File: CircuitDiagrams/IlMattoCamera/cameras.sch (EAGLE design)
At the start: 19 parts, among them Q1 12MHz, U1 ATMEGA644-20PU, X1 SDBMF

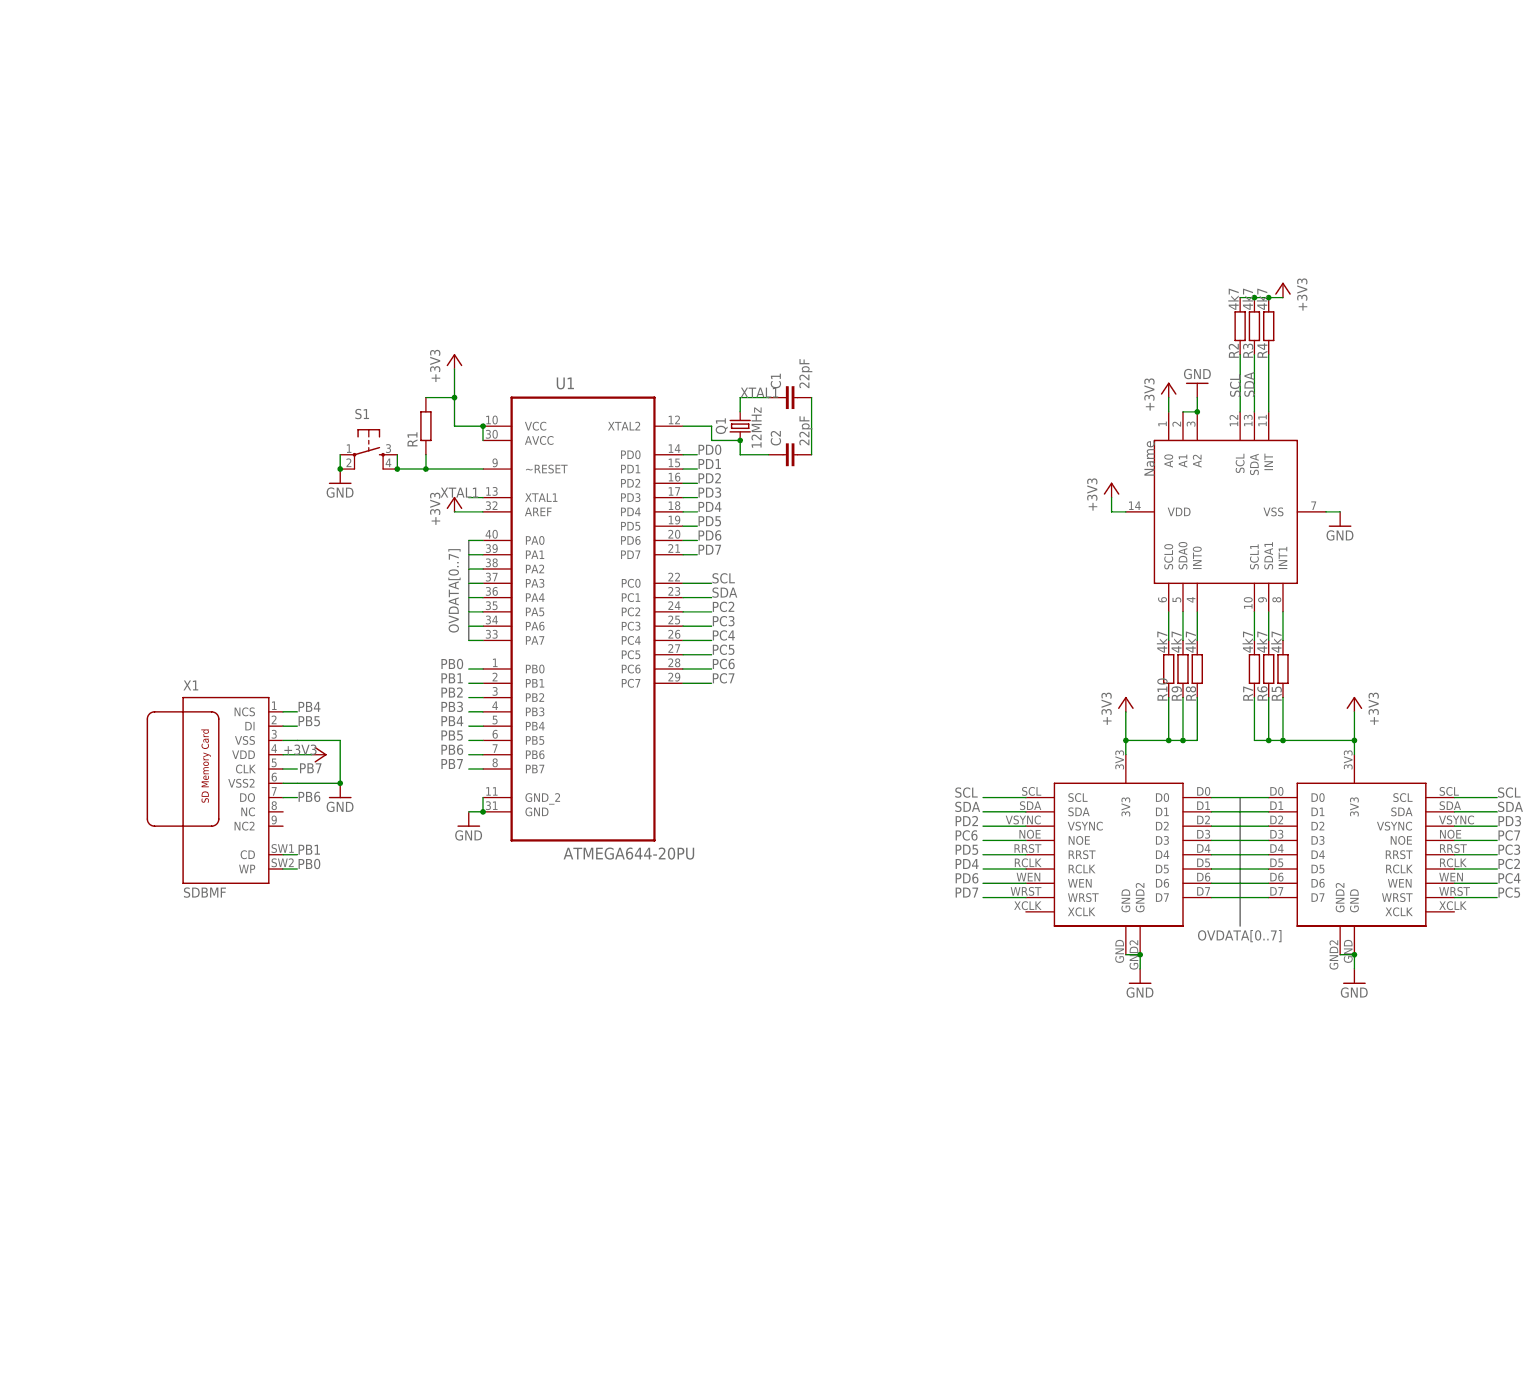
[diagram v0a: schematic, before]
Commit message: Finished Circuit Diagram of Il Matto Camera Platform
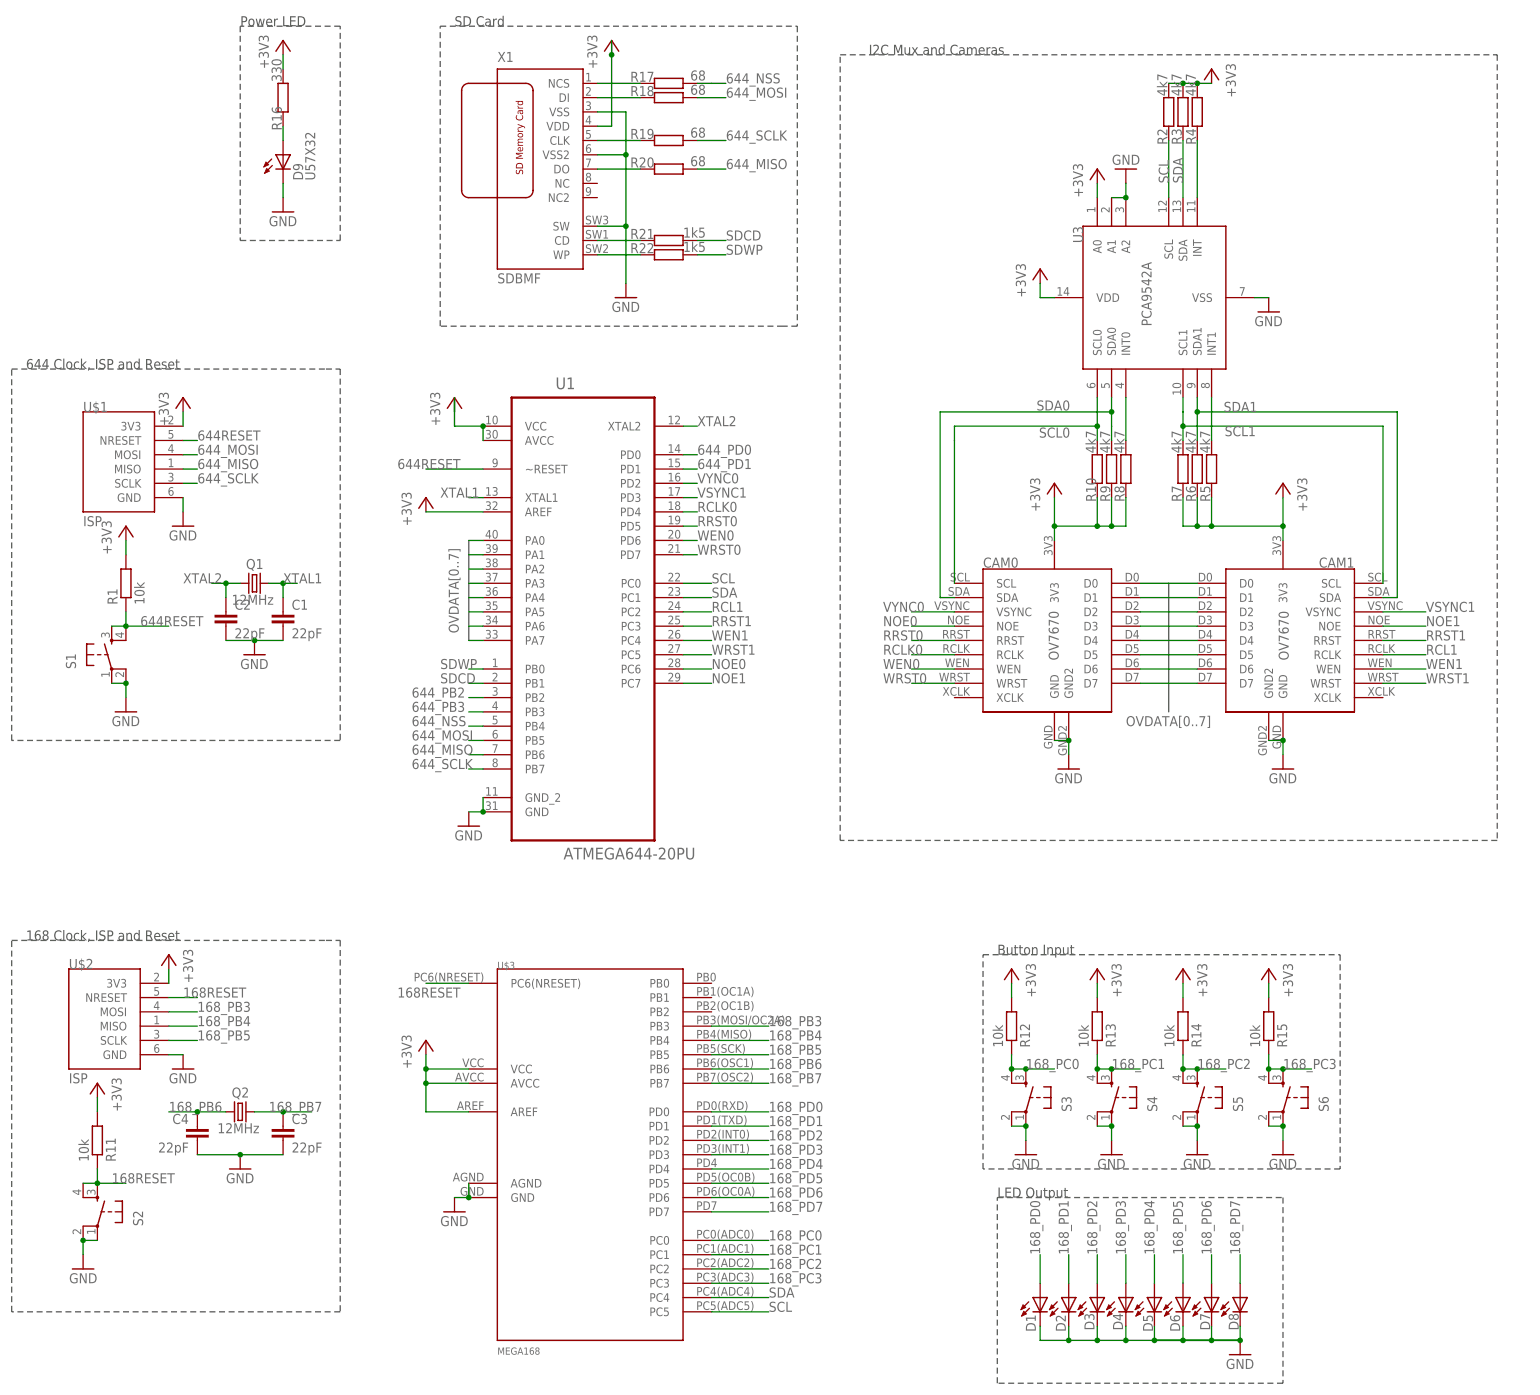
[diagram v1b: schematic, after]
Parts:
- added C3, C4: 22pF, resistor:C-EU025-040X050
- added CAM0, CAM1: OV7670, seblov:OV7670
- added D1, D2, D3, D4, D5, D6, D7, D8, D9: U57X32, led:U57X32
- added Q2: 12MHz, crystal:CRYSTALHC49S
- added R11, R12, R13, R14, R15: 10k, resistor:R-EU_0204/7
- added R16: 330, resistor:R-EU_0204/7
- added R17, R18, R19, R20: 68, resistor:R-EU_0204/7
- added R21, R22: 1k5, resistor:R-EU_0204/7
- added S2, S3, S4, S5, S6: (no value), SparkFun:TAC_SWITCHPTH
- added U3: PCA9542A, seblov:PCA9542A
- R1: value (none) -> 10k
- U$1, U$2: value OV7670 -> ISP; device seblov:OV7670 -> seblov:ISP
- U$3: value PCA9542A -> MEGA168; device seblov:PCA9542A -> seblov:MEGA168
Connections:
- net N$10 renamed XTAL2
- net PB2 renamed 644_PB2
- net PB3 renamed 644_PB3
- net PD0 renamed 644_PD0
- net PD1 renamed 644_PD1
- removed net N$2: R1.1, S1.3, S1.4, U1.~RESET
- removed net N$3: R6.2, U$3.SDA1
- removed net N$4: R7.2, U$3.SCL1
- removed net N$6: R9.2, U$3.SDA0
- removed net N$7: R10.2, U$3.SCL0
- removed net N$9: C1.2, C2.2
- removed net PB0: U1.PB0, X1.WP
- removed net PB1: U1.PB1, X1.CD
- removed net PB4: U1.PB4, X1.NCS
- removed net PB5: U1.PB5, X1.DI
- removed net PB6: U1.PB6, X1.DO
- removed net PB7: U1.PB7, X1.CLK
- removed net PC2: U$2.RCLK, U1.PC2
- removed net PC3: U$2.RRST, U1.PC3
- removed net PC4: U$2.WEN, U1.PC4
- removed net PC5: U$2.WRST, U1.PC5
- removed net PC6: U$1.NOE, U1.PC6
- removed net PC7: U$2.NOE, U1.PC7
- removed net PD2: U$1.VSYNC, U1.PD2
- removed net PD3: U$2.VSYNC, U1.PD3
- removed net PD4: U$1.RCLK, U1.PD4
- removed net PD5: U$1.RRST, U1.PD5
- removed net PD6: U$1.WEN, U1.PD6
- removed net PD7: U$1.WRST, U1.PD7
- new net 168RESET: R11.1, S2.3, S2.4, U$2.NRESET, U$3.PC6(NRESET)
- new net 168_PB3: U$2.MOSI, U$3.PB3
- new net 168_PB4: U$2.MISO, U$3.PB4
- new net 168_PB5: U$2.SCLK, U$3.PB5
- new net 168_PB6: C4.1, Q2.1, U$3.PB6
- new net 168_PB7: C3.1, Q2.2, U$3.PB7
- new net 168_PC0: R12.1, S3.3, S3.4, U$3.PC0
- new net 168_PC1: R13.1, S4.3, S4.4, U$3.PC1
- new net 168_PC2: R14.1, S5.3, S5.4, U$3.PC2
- new net 168_PC3: R15.1, S6.3, S6.4, U$3.PC3
- new net 168_PD0: D1.A, U$3.PD0
- new net 168_PD1: D2.A, U$3.PD1
- new net 168_PD2: D3.A, U$3.PD2
- new net 168_PD3: D4.A, U$3.PD3
- new net 168_PD4: D5.A, U$3.PD4
- new net 168_PD5: D6.A, U$3.PD5
- new net 168_PD6: D7.A, U$3.PD6
- new net 168_PD7: D8.A, U$3.PD7
- new net 644RESET: R1.1, S1.3, S1.4, U$1.NRESET, U1.~RESET
- new net 644_MISO: R20.1, U$1.MISO, U1.PB6
- new net 644_MOSI: R18.1, U$1.MOSI, U1.PB5
- new net 644_NSS: R17.1, U1.PB4
- new net 644_SCLK: R19.1, U$1.SCLK, U1.PB7
- new net N$13: R17.2, X1.NCS
- new net N$27: R18.2, X1.DI
- new net N$28: D9.A, R16.1
- new net N$29: R19.2, X1.CLK
- new net N$30: R20.2, X1.DO
- new net N$31: R21.2, X1.CD
- new net N$32: R22.2, X1.WP
- new net NOE0: CAM0.NOE, U1.PC6
- new net NOE1: CAM1.NOE, U1.PC7
- new net RCL1: CAM1.RCLK, U1.PC2
- new net RCLK0: CAM0.RCLK, U1.PD4
- new net RRST0: CAM0.RRST, U1.PD5
- new net RRST1: CAM1.RRST, U1.PC3
- new net SCL0: CAM0.SCL, R10.2, U3.SCL0
- new net SCL1: CAM1.SCL, R7.2, U3.SCL1
- new net SDA0: CAM0.SDA, R9.2, U3.SDA0
- new net SDA1: CAM1.SDA, R6.2, U3.SDA1
- new net SDCD: R21.1, U1.PB1
- new net SDWP: R22.1, U1.PB0
- new net VSYNC1: CAM1.VSYNC, U1.PD3
- new net VYNC0: CAM0.VSYNC, U1.PD2
- new net WEN0: CAM0.WEN, U1.PD6
- new net WEN1: CAM1.WEN, U1.PC4
- new net WRST0: CAM0.WRST, U1.PD7
- new net WRST1: CAM1.WRST, U1.PC5
- net +3V3: now also CAM0.3V3, CAM1.3V3, R11.2, R12.2, R13.2, R14.2, R15.2, R16.2, U$3.AREF, U$3.AVCC, U$3.VCC, U3.A0, U3.VDD; no longer U$3.A0, U$3.VDD
- net GND: now also C1.2, C2.2, C3.2, C4.2, CAM0.GND, CAM0.GND2, CAM1.GND, CAM1.GND2, D1.C, D2.C, D3.C, D4.C, D5.C, D6.C, D7.C, D8.C, D9.C, S2.1, S2.2, S3.1, S3.2, S4.1, S4.2, S5.1, S5.2, S6.1, S6.2, U$3.AGND, U$3.GND, U3.A1, U3.A2, U3.VSS, X1.SW; no longer U$1.GND2, U$2.GND2, U$3.A1, U$3.A2, U$3.VSS
- net N$1: now also U3.INT1; no longer U$3.INT1
- net N$5: now also U3.INT0; no longer U$3.INT0
- net N$8: now also U3.INT; no longer U$3.INT
- net OVDATA0: now also CAM0.D0, CAM1.D0; no longer U$1.D0, U$2.D0
- net OVDATA1: now also CAM0.D1, CAM1.D1; no longer U$1.D1, U$2.D1
- net OVDATA2: now also CAM0.D2, CAM1.D2; no longer U$1.D2, U$2.D2
- net OVDATA3: now also CAM0.D3, CAM1.D3; no longer U$1.D3, U$2.D3
- net OVDATA4: now also CAM0.D4, CAM1.D4; no longer U$1.D4, U$2.D4
- net OVDATA5: now also CAM0.D5, CAM1.D5; no longer U$1.D5, U$2.D5
- net OVDATA6: now also CAM0.D6, CAM1.D6; no longer U$1.D6, U$2.D6
- net OVDATA7: now also CAM0.D7, CAM1.D7; no longer U$1.D7, U$2.D7
- net SCL: now also U$3.PC5, U3.SCL; no longer U$1.SCL, U$2.SCL, U$3.SCL
- net SDA: now also U$3.PC4, U3.SDA; no longer U$1.SDA, U$2.SDA, U$3.SDA
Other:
- note added: "168 Clock, ISP and Reset"
- note added: "644 Clock, ISP and Reset"
- note added: "Button Input"
- note added: "I2C Mux and Cameras"
- note added: "LED Output"
- note added: "Power LED"
- note added: "SD Card"
- moved on the sheet: C1, C2, Q1, R1, R10, R2, R3, R4, R5, R6, R7, R8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
